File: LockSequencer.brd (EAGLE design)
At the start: 80.3 x 77.5 mm, 78 parts, among them IC1 4017D, IC2 NE555, K1 G2RATE-OJ, K2 G2RATE-OJ

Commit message: Nearly completed second revision
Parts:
- removed H2: MOUNT-HOLE2.8, holes:2,8
- added H3: MOUNT-PAD-ROUND2.8, holes:2,8-PAD
- H1: value MOUNT-HOLE2.8 -> MOUNT-PAD-ROUND2.8; device holes:2,8 -> holes:2,8-PAD
- moved C11 18.6 mm to (43.7, 56.5), turned to 45 degrees
- moved X10 17.3 mm to (37.5, 67.9)
- moved F1 17.3 mm to (24.8, 69.2), turned to 0 degrees
- moved D1 15.3 mm to (44.5, 32.4), turned to 0 degrees
- moved R12 11.0 mm to (43.2, 41.9), turned to 180 degrees
- moved R9 10.2 mm to (29.2, 57.1)
- moved R11 10.2 mm to (55.2, 10.8)
- moved X2 9.71 mm to (9.53, 67.9), turned to 180 degrees
- moved C1 9.25 mm to (25.4, 62.2), turned to 90 degrees
- moved R10 8.26 mm to (54.0, 24.8), turned to 135 degrees
- moved C7 7.43 mm to (26.7, 55.9), turned to 270 degrees
- moved LED1 7.43 mm to (36.8, 37.5), turned to 90 degrees
- moved T3 6.99 mm to (53.3, 15.2), turned to 0 degrees
- moved D2 6.98 mm to (45.7, 20.3)
- moved D7 6.54 mm to (19.1, 64.1)
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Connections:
- net N$27: now also K1.1; no longer K1.2
- net VSUPPLY: now also K1.2; no longer K1.1
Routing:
- net VSS: track 12.2 -> 74.0 mm, vias 2 -> 1
- net N$27: track 31.4 -> 16.6 mm
- net N$15: track 15.5 -> 2.52 mm
- net N$43: track 28.1 -> 40.5 mm
- net OPEN: track 16.0 -> 26.5 mm
- net LATCH: track 21.2 -> 29.4 mm
- net N$19: track 9.40 -> 3.70 mm
- net N$18: track 16.3 -> 20.4 mm
- net N$11: track 6.30 -> 9.98 mm
- net VDD: track 63.0 -> 59.8 mm, vias 3 -> 0
- net N$40: track 10.7 -> 13.3 mm
- net VSUPPLY: track 88.5 -> 86.7 mm, vias 1 -> 0
- net N$39: track 0.63 -> 2.28 mm
- net N$21: track 54.8 -> 56.2 mm
- net N$8: track 4.71 -> 5.87 mm
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- removed copper zone on layer 1, net VDD
- removed copper zone on layer 1, net VSUPPLY

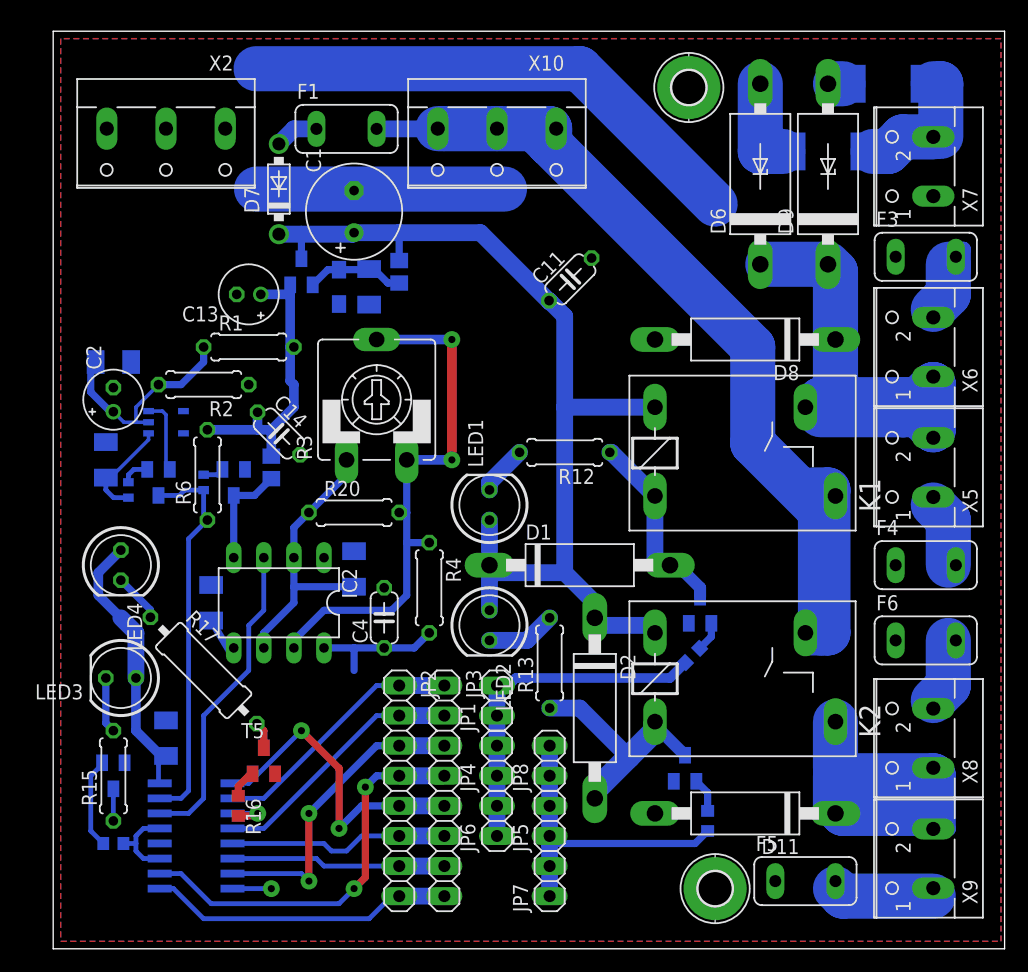
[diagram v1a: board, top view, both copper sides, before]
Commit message: Nearly finished on second revision - ground and power resrouted on right side of board. 4017 and 55 nearly done.
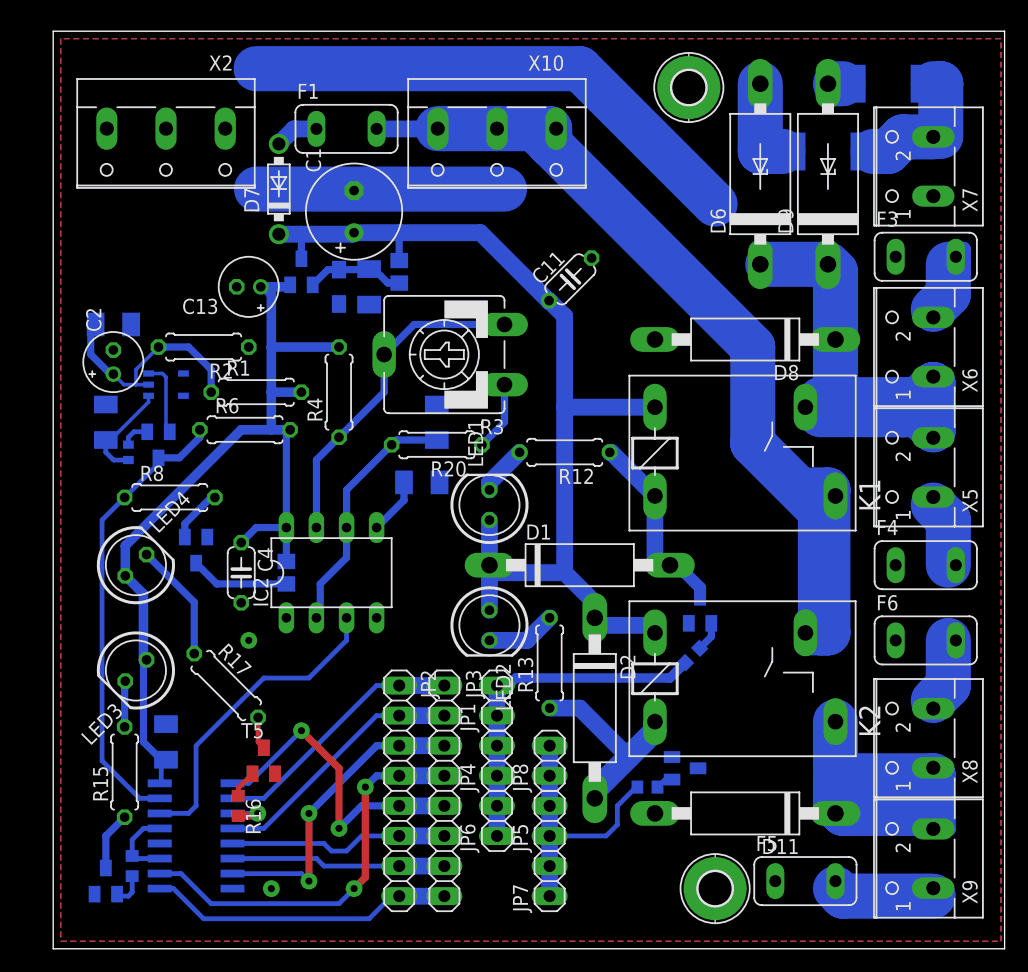
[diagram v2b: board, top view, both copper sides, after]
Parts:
- removed C14: 100n, rcl:C050-024X044
- R17: device rcl:0309/12 -> rcl:0207/7
- R20: value 100k -> 51k
- R3: value 220K -> 100K
- R8: device rcl:R0402 -> rcl:0207/7
- moved C5 20.5 mm to (31.1, 39.4), turned to 180 degrees
- moved R4 18.2 mm to (24.1, 47.0), turned to 90 degrees
- moved C6 14.2 mm to (32.4, 44.5)
- moved C4 12.7 mm to (15.9, 31.8), turned to 270 degrees
- moved R20 9.03 mm to (32.4, 42.5), turned to 180 degrees
- moved R7 8.98 mm to (19.7, 31.8)
- moved T1 8.91 mm to (4.45, 5.71), turned to 0 degrees
- moved R3 6.87 mm to (33.0, 50.2), turned to 90 degrees
- moved U$1 6.54 mm to (12.1, 33.7)
- moved R11 5.83 mm to (50.2, 13.7), turned to 180 degrees
- moved IC2 5.12 mm to (23.5, 31.8), turned to 0 degrees
- moved R6 4.96 mm to (16.2, 43.8), turned to 0 degrees
- moved R1 3.86 mm to (17.1, 47.0)
- moved C12 3.18 mm to (4.45, 44.5)
- moved C2 3.18 mm to (5.08, 49.5)
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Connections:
- removed net N$24: IC2.7, R20.2, R3.E, R3.S, R4.1
- new net N$29: IC2.7, R3.E, R3.S, R4.1
- new net N$31: R20.1, R3.A
- net N$14: now also R20.2; no longer R20.1, R3.A
- net VDD: no longer C14.1
- net VSS: no longer C14.2
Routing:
- net N$24: track 46.0 -> 0.00 mm, vias 2 -> 0
- net N$29: track 0.00 -> 28.2 mm
- net VDD: track 59.8 -> 79.7 mm
- net N$31: track 0.00 -> 5.87 mm
- net N$13: track 4.16 -> 10.0 mm
- net RESET: track 33.1 -> 39.0 mm
- net N$16: track 7.65 -> 2.95 mm
- net OPEN: track 26.5 -> 22.7 mm
- net VSS: track 74.0 -> 70.8 mm, vias 1 -> 2
- net N$18: track 20.4 -> 17.4 mm
- net N$28: track 1.78 -> 4.58 mm
- net N$14: track 23.8 -> 21.2 mm
- net N$33: track 2.71 -> 4.96 mm
- net N$26: track 2.89 -> 0.90 mm
- net N$2: track 19.0 -> 20.2 mm
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
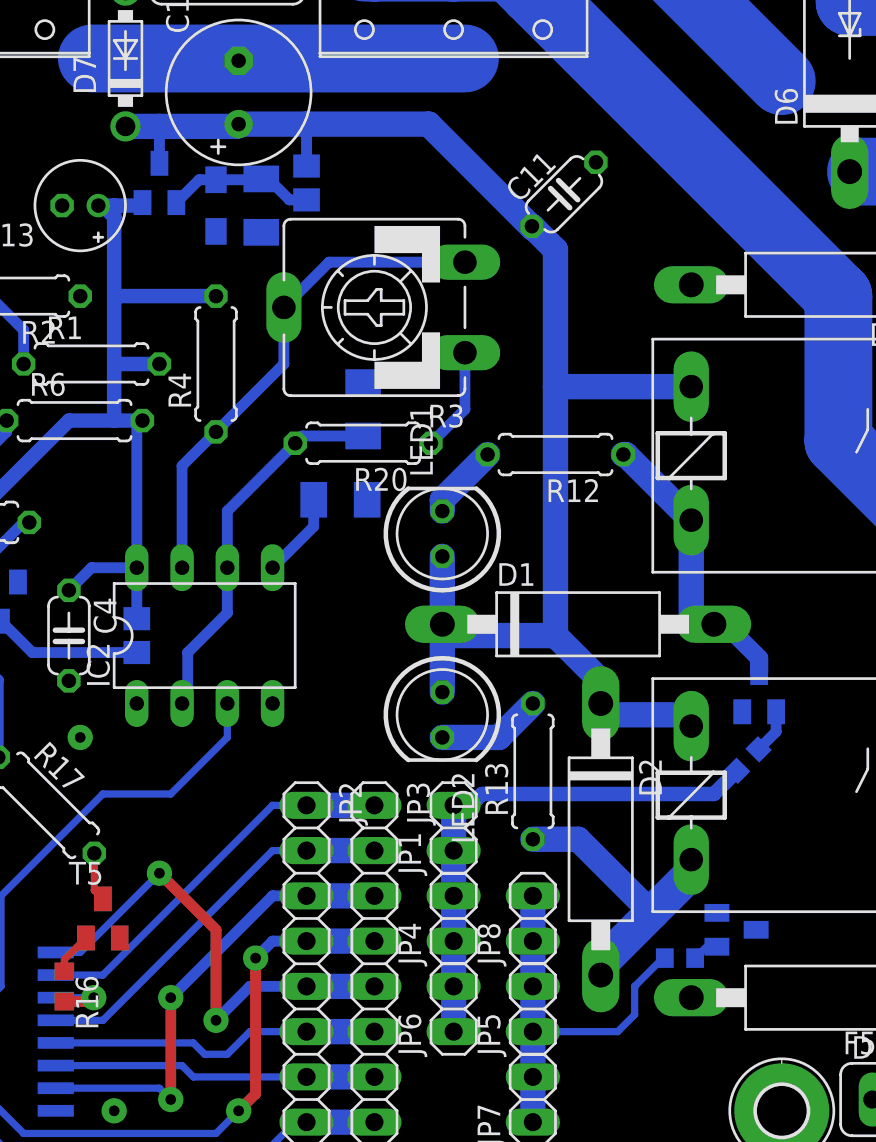
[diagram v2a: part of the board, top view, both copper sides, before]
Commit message: Finished relayout ot RHS
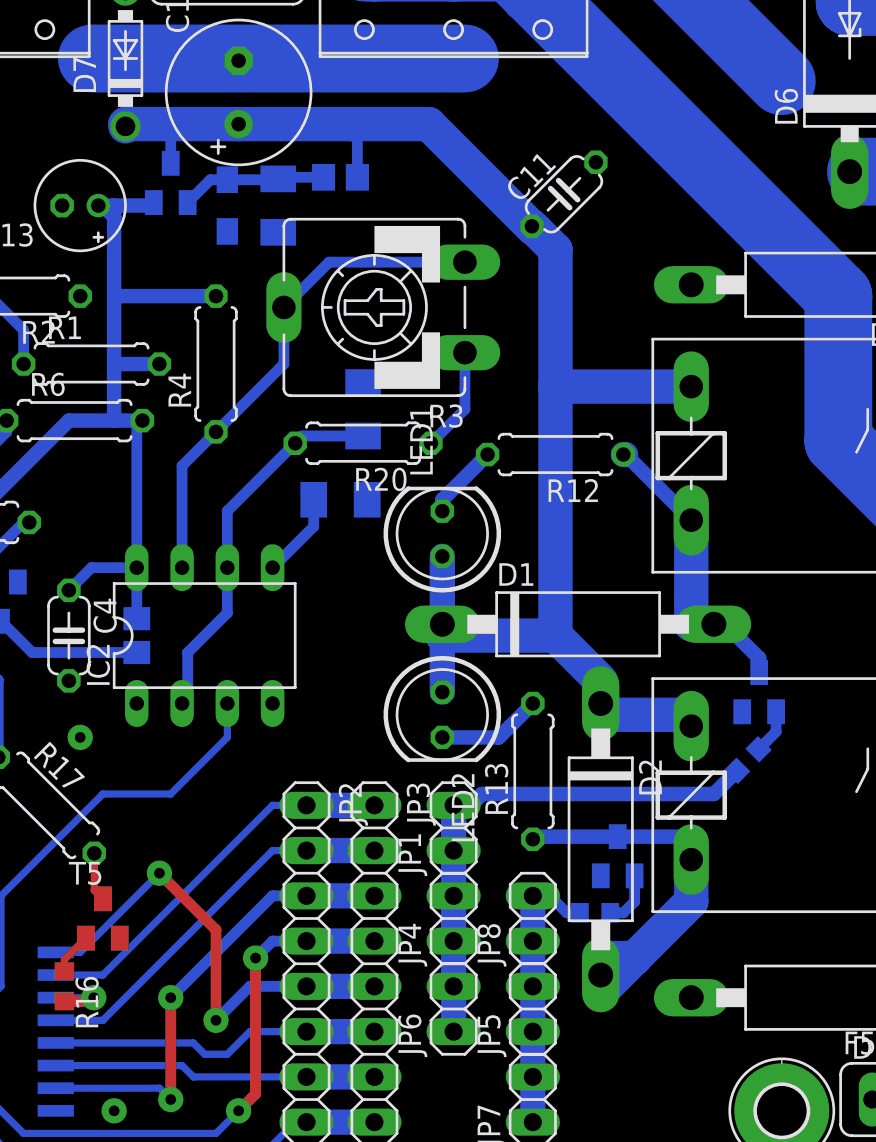
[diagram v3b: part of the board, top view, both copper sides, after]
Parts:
- moved T3 7.84 mm to (46.7, 19.4), turned to 0 degrees
- moved R11 5.40 mm to (45.4, 16.2)
- moved R9 1.93 mm to (31.1, 57.5), turned to 180 degrees
- moved C7 0.95 mm to (27.6, 55.9)
- moved D3 0.64 mm to (24.8, 55.9)
- moved T2 0.64 mm to (21.6, 57.1)
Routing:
- net OPEN: track 22.7 -> 15.7 mm
- net N$18: track 17.4 -> 23.7 mm
- net N$26: track 0.90 -> 3.08 mm
- net VSUPPLY: track 86.7 -> 87.7 mm
- net VDD: track 79.7 -> 80.2 mm

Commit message: Second revision complete minus DRC
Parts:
- removed D6, D9: UF5404, diode:CB429-15
- added D4: (no value), diode:CB429-15R
- added D5: (no value), diode:CB429-15V
- D1, D11, D2, D8: value P6KEXXC -> P6KEXXCTS-P6KE; device diode:CB417-15 -> diode:DO15-10
- moved F4 36.4 mm to (63.5, 67.3)
- moved R19 32.7 mm to (71.1, 40.3), turned to 90 degrees
- moved X7 32.7 mm to (73.0, 33.3)
- moved R18 29.0 mm to (75.9, 40.3), turned to 90 degrees
- moved C11 25.4 mm to (45.1, 31.1), turned to 0 degrees
- moved C5 20.0 mm to (21.3, 21.9), turned to 270 degrees
- moved X5 19.0 mm to (73.0, 59.7)
- moved X6 19.0 mm to (73.0, 69.8)
- moved C6 18.0 mm to (29.5, 26.7), turned to 225 degrees
- moved F3 17.3 mm to (63.5, 72.4)
- moved D1 9.66 mm to (46.0, 41.9), turned to 270 degrees
- moved D8 9.38 mm to (62.2, 60.0)
- moved R4 8.91 mm to (23.5, 38.1), turned to 180 degrees
- moved R20 8.09 mm to (30.8, 34.6), turned to 270 degrees
- moved R12 7.94 mm to (43.5, 34.0)
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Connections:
- removed net N$39: D9.A, R19.2
- new net N$24: IC2.7, R3.A, R4.1
- net N$21: now also D4.C, D5.C, X5.1; no longer D6.C, D9.C, X6.1
- net N$29: now also D4.A, R18.2; no longer IC2.7, R3.E, R3.S, R4.1
- net N$30: now also X6.1; no longer X5.1
- net N$31: now also R3.E, R3.S; no longer R3.A
- net N$37: now also D5.A, R19.2; no longer D6.A, R18.2
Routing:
- net VSS: track 70.8 -> 98.7 mm, vias 2 -> 4
- net N$29: track 28.2 -> 2.91 mm
- net N$21: track 56.2 -> 37.0 mm
- net N$24: track 0.00 -> 19.1 mm
- net N$31: track 5.87 -> 18.8 mm
- net RESET_N: track 8.35 -> 20.4 mm
- net N$18: track 23.7 -> 14.4 mm
- net VEXTERNAL: track 90.7 -> 82.8 mm
- net N$37: track 8.63 -> 2.91 mm
- net N$40: track 13.3 -> 8.45 mm
- net CLOCK: track 26.7 -> 22.8 mm
- net N$14: track 21.2 -> 17.9 mm
- net N$15: track 2.52 -> 4.94 mm
- net N$39: track 2.28 -> 0.00 mm
- net N$10: track 4.23 -> 6.40 mm
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
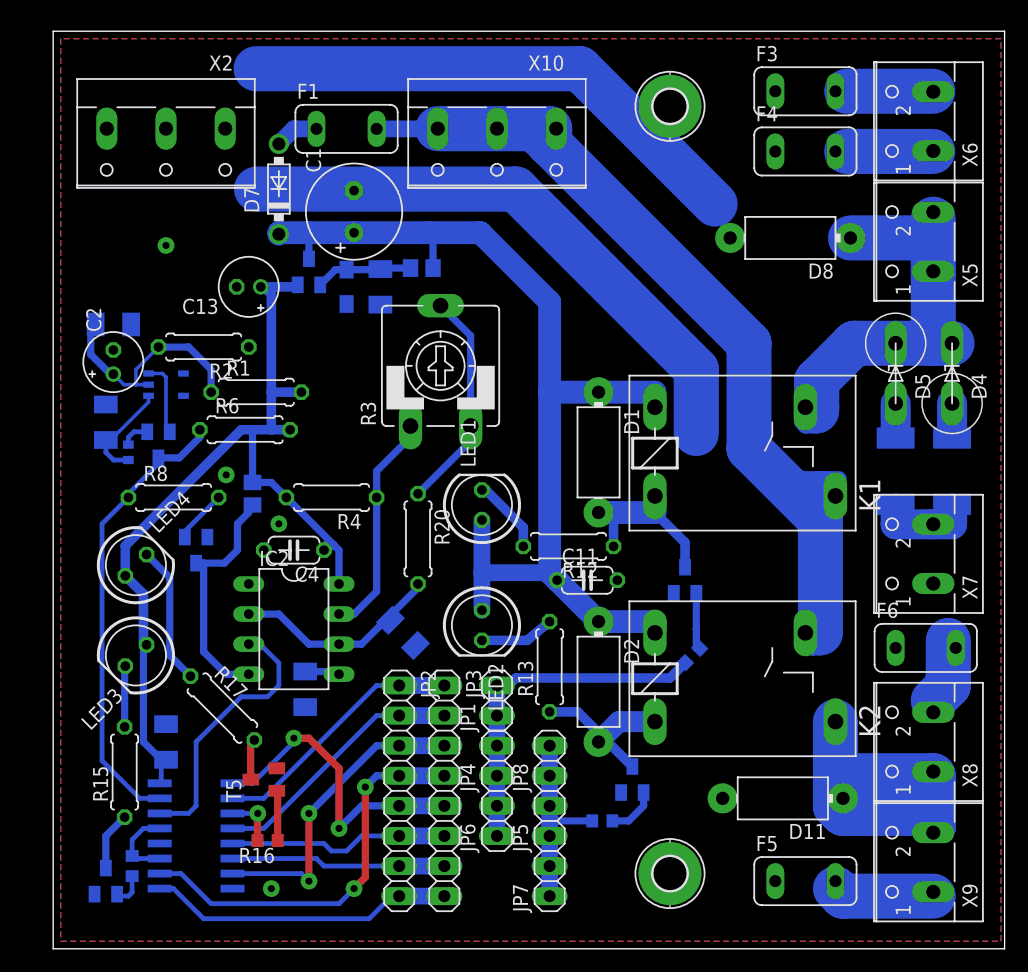
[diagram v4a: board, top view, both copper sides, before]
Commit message: Completed tweaks to second revision including new package for 1N5819. Ready for printing.
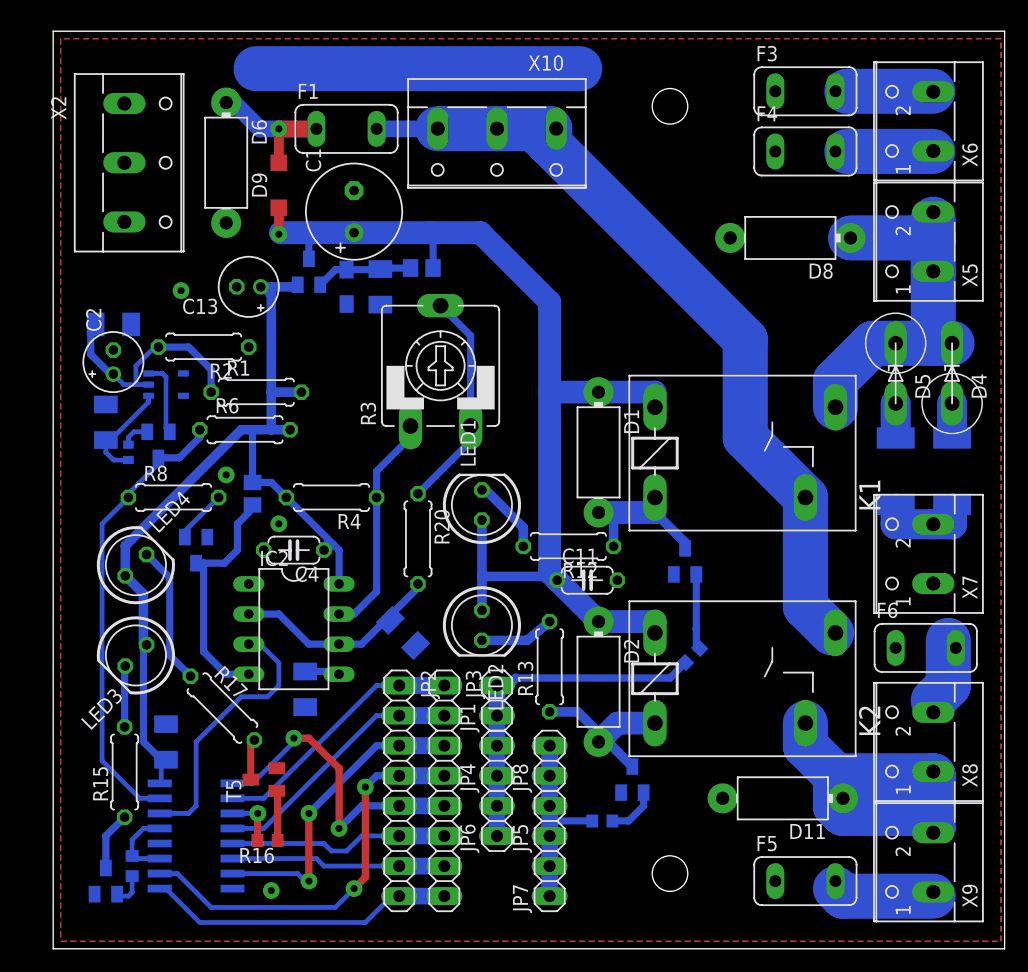
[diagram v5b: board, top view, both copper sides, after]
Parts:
- removed D7: 1N5819-T, diode:DO41-7.6
- removed H1, H3: MOUNT-PAD-ROUND2.8, holes:2,8-PAD
- added D6: P6KEXXCTS-P6KE, diode:DO15-10
- added D9: (no value), diode:SOD123
- D4, D5: value (none) -> UF5404
- R13: value 15K4 -> 2K2
- moved X2 2.73 mm to (7.30, 66.4), turned to 270 degrees
- moved T4 1.59 mm to (53.3, 32.7)
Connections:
- removed net N$19: D7.A, F1.1
- new net VEXTERNAL-FUSED: D6.C, D9.A, F1.1
- net VSS: now also D6.A
- net VSUPPLY: now also D9.C; no longer D7.C
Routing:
- net VSS: track 98.7 -> 33.7 mm
- net VEXTERNAL-FUSED: track 0.00 -> 14.6 mm, vias 0 -> 1
- net VEXTERNAL: track 82.8 -> 70.3 mm
- net N$21: track 37.0 -> 31.4 mm
- net N$19: track 3.70 -> 0.00 mm
- net VSUPPLY: track 88.6 -> 91.7 mm, vias 0 -> 1
- net N$27: track 14.7 -> 13.0 mm
- net N$15: track 4.94 -> 6.52 mm
- net N$43: track 41.0 -> 42.6 mm

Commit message: Extra revision following minor assembly problems
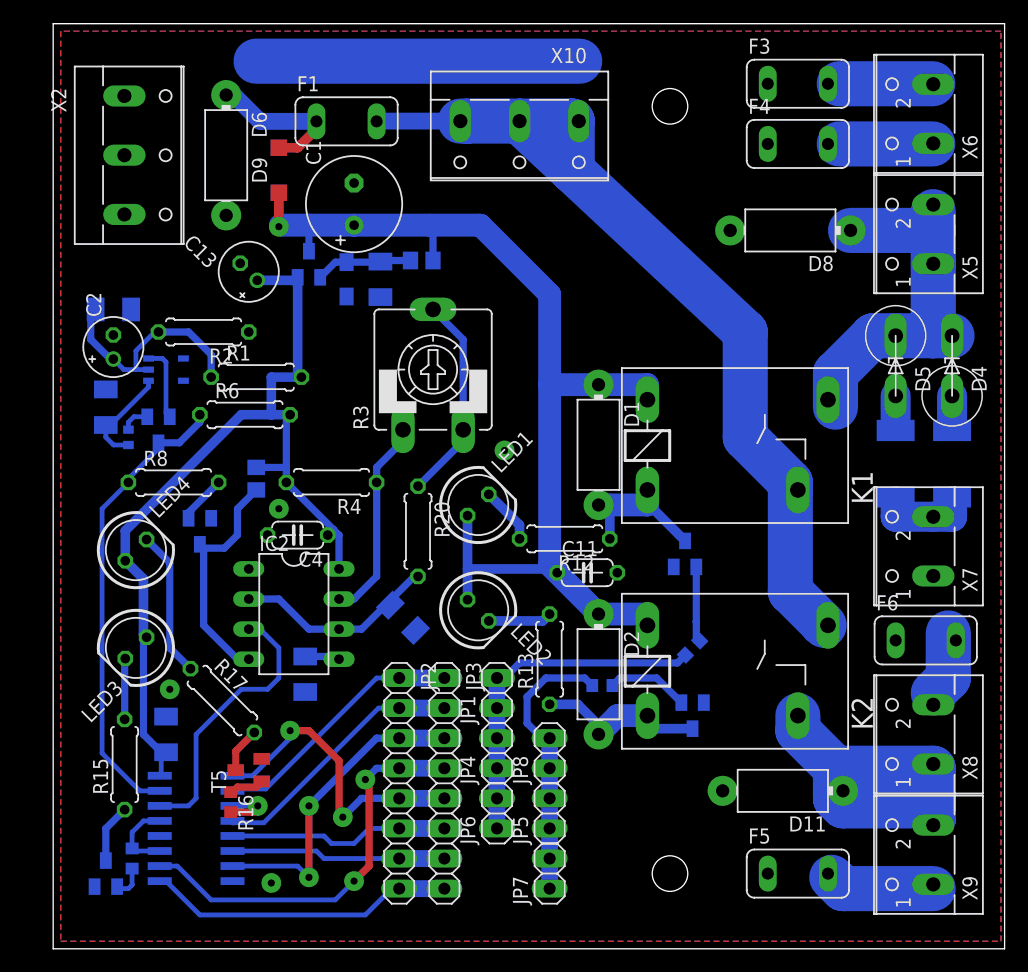
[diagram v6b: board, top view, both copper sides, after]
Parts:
- R3: value 100K -> 220K
- moved R11 11.4 mm to (46.4, 22.2)
- moved T3 7.41 mm to (54.0, 19.7), turned to 180 degrees
- moved R16 4.49 mm to (15.0, 12.4), turned to 270 degrees
- moved X10 2.01 mm to (39.4, 68.6)
- moved U$1 1.62 mm to (12.4, 35.2)
- moved T5 1.50 mm to (16.5, 15.1)
- moved R7 1.31 mm to (17.1, 39.7)
- moved LED2 1.31 mm to (35.9, 28.6), turned to 315 degrees
- moved C4 1.31 mm to (20.6, 34.9)
- moved C9 1.27 mm to (5.08, 54.0)
- moved LED4 1.27 mm to (6.99, 33.7)
- moved R2 1.27 mm to (12.7, 52.1)
- moved R5 1.27 mm to (6.35, 43.2)
- moved R6 1.27 mm to (16.2, 45.1)
- moved U$4 1.27 mm to (9.53, 48.9)
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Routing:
- net OPEN: track 16.9 -> 24.1 mm
- net VEXTERNAL: track 70.3 -> 76.1 mm
- net N$26: track 4.29 -> 6.94 mm
- net N$24: track 19.1 -> 17.3 mm
- net N$10: track 6.40 -> 4.83 mm
- net VEXTERNAL-FUSED: track 14.6 -> 13.0 mm, vias 1 -> 0
- net N$21: track 31.4 -> 33.0 mm
- net N$31: track 18.8 -> 17.6 mm
- net N$8: track 6.29 -> 5.37 mm
- net N$36: track 4.22 -> 3.31 mm
- net N$27: track 13.0 -> 13.9 mm
- net N$17: track 3.46 -> 4.26 mm
- net N$18: track 14.3 -> 15.1 mm
- net N$22: track 9.51 -> 10.2 mm
- net VDD: track 78.1 -> 77.4 mm
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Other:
- board size 80.3 x 77.5 mm -> 80.3 x 78.1 mm
